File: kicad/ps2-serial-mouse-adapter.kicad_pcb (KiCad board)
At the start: 2 copper layers, 60.5 x 31.5 mm, 13 parts, among them U1 Arduino_Mini, U2 MAX232

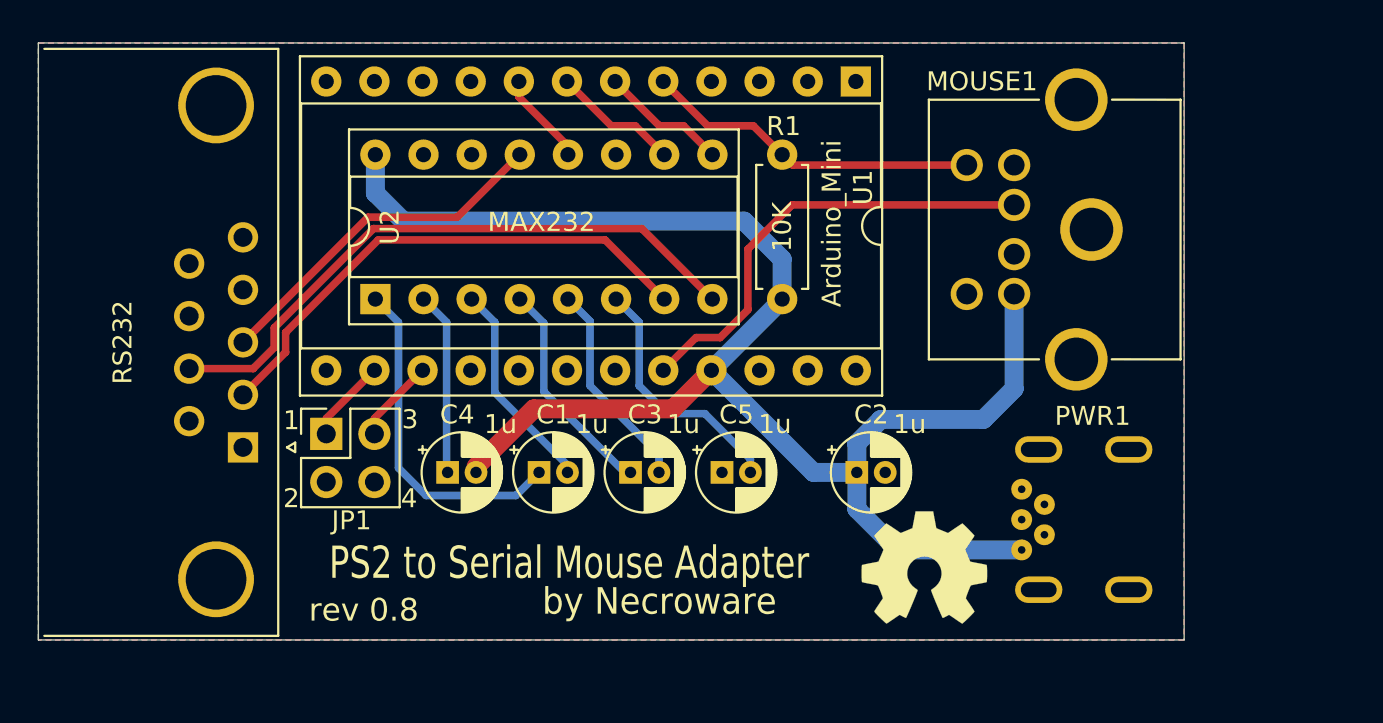
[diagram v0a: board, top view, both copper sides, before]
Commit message: Add footprints for Arduino Nano socket and MAX3232 HW-027 module
- Created a new footprint for the Arduino Nano socket with 2x15 pin configuration, including through-hole pads and silk screen details.
- Added a footprint for the MAX3232 HW-027 module featuring castellated pads, through-hole and SMD pads, along with necessary fabrication outlines.
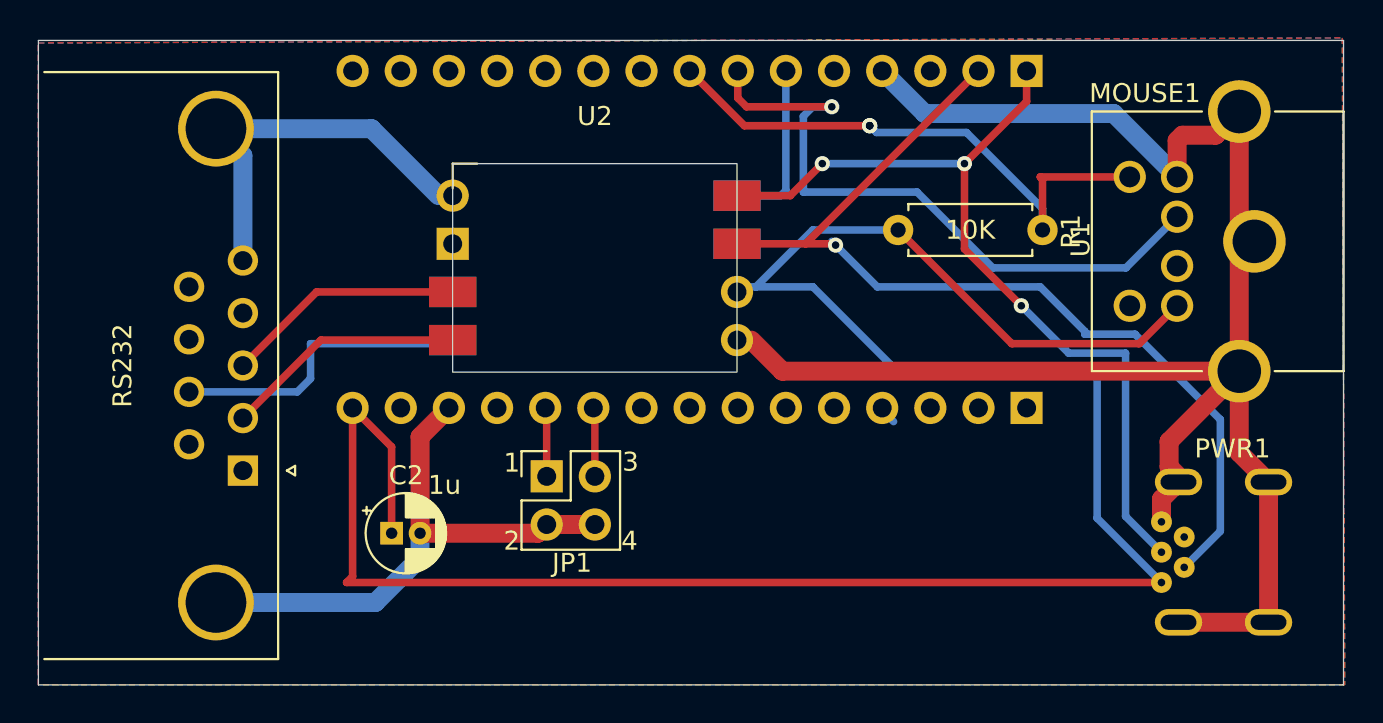
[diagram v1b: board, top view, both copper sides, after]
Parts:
- removed C1, C3, C4, C5: 1u, Capacitor_THT:CP_Radial_D4.0mm_P1.50mm
- removed REF**: OSHW-Symbol_6.7x6mm_SilkScreen, Symbol:OSHW-Symbol_6.7x6mm_SilkScreen
- U1: value Arduino_Mini -> Arduino_Nano; footprint Package_DIP:DIP-24_W15.24mm_Socket -> ps2-serial-mouse-adapter:Arduino_Nano_Socket
- U2: value MAX232 -> MAX3232_HW027; footprint Package_DIP:DIP-16_W7.62mm_Socket -> ps2-serial-mouse-adapter:MAX3232_HW027
- moved C2 24.8 mm to (99.9, 80.7)
- moved U1 12.1 mm to (115.6, 65.2)
- moved JP1 11.8 mm to (108.1, 77.7)
- moved U2 11.7 mm to (110.6, 66.7), turned to 0 degrees
- moved MOUSE1 8.62 mm to (138.9, 68.7)
- moved PWR1 7.57 mm to (140.5, 81.7)
- moved R1 7.12 mm to (126.6, 64.7), turned to 0 degrees
- moved RS232 1.23 mm to (92.1, 77.4)
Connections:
- C2 pad 1: Net-(PWR1-VBUS) -> unconnected-(C2-Pad1)
- JP1 pad 1: Net-(JP1-Pin_1) -> unconnected-(C2-Pad1)
- JP1 pad 3: Net-(JP1-Pin_3) -> unconnected-(C2-Pad1)
- MOUSE1 pad 4: Net-(PWR1-VBUS) -> unconnected-(C2-Pad1)
- PWR1 pad 1: Net-(PWR1-VBUS) -> unconnected-(C2-Pad1)
- PWR1 pad 2: unconnected-(PWR1-D--Pad2) -> RX
- PWR1 pad 3: unconnected-(PWR1-D+-Pad3) -> TX
- R1 pad 1: Net-(PWR1-VBUS) -> unconnected-(C2-Pad1)
- RS232 pad 2: Net-(U2-T2OUT) -> Net-(U2-RS232_TXD1)
- RS232 pad 3: Net-(U2-R1IN) -> Net-(U2-RS232_RXD1)
- RS232 pad 7: Net-(U2-R2IN) -> Net-(U2-RS232_RXD2)
- U1 pad 1: unconnected-(U1-TX/D0-Pad1) -> TX
- U1 pad 14: Net-(JP1-Pin_1) -> unconnected-(U1-D11-Pad14)
- U1 pad 15: Net-(JP1-Pin_3) -> unconnected-(U1-D12-Pad15)
- U1 pad 16: unconnected-(U1-D13-Pad16) -> unconnected-(C2-Pad1)
- U1 pad 17: unconnected-(U1-A0-Pad17) -> unconnected-(C2-Pad1)
- U1 pad 18: unconnected-(U1-A1-Pad18) -> unconnected-(C2-Pad1)
- U1 pad 19: unconnected-(U1-A2-Pad19) -> unconnected-(C2-Pad1)
- U1 pad 2: unconnected-(U1-RX/D1-Pad2) -> RX
- U1 pad 20: DATA -> unconnected-(C2-Pad1)
- U1 pad 21: Net-(PWR1-VBUS) -> unconnected-(C2-Pad1)
- U1 pad 22: unconnected-(U1-RST-Pad22) -> unconnected-(C2-Pad1)
- U1 pad 23: GND -> unconnected-(C2-Pad1)
- U1 pad 24: unconnected-(U1-VIN-Pad24) -> unconnected-(C2-Pad1)
- U1 pad 5: CLK -> unconnected-(U1-D2-Pad5)
- U1 pad 7: TX -> DATA
- U1 pad 8: RX -> CLK
- U2 pad 1: Net-(U2-C1+) -> unconnected-(C2-Pad1)
- U2 pad 10: TX -> RX
- U2 pad 12: RX -> RTS
- U2 pad 2: Net-(U2-VS+) -> GND
- U2 pad 3: Net-(U2-C1-) -> unconnected-(C2-Pad1)
- U2 pad 4: Net-(U2-C2+) -> GND
- U2 pad 5: Net-(U2-C2-) -> Net-(U2-RS232_RXD1)
- U2 pad 6: Net-(U2-VS-) -> Net-(U2-RS232_TXD1)
- U2 pad 7: Net-(U2-T2OUT) -> Net-(U2-RS232_RXD2)
- U2 pad 8: Net-(U2-R2IN) -> unconnected-(U2-RS232_TXD2-Pad8)
- U2 pad 9: RTS -> TX
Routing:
- net GND: track 0.00 -> 143.5 mm
- net unconnected-(C2-Pad1): track 0.00 -> 129.0 mm
- net Net-(PWR1-VBUS): track 84.3 -> 0.00 mm
- net RX: track 4.93 -> 50.7 mm, vias 0 -> 1
- net TX: track 6.73 -> 45.1 mm, vias 0 -> 3
- net Net-(U2-R2IN): track 32.8 -> 0.00 mm
- net Net-(U2-T2OUT): track 27.5 -> 0.00 mm
- net Net-(U2-R1IN): track 18.7 -> 0.00 mm
- net Net-(U2-C1+): track 17.9 -> 0.00 mm
- net Net-(U2-RS232_RXD2): track 0.00 -> 15.8 mm
- net Net-(U2-VS-): track 13.2 -> 0.00 mm
- net Net-(U2-RS232_TXD1): track 0.00 -> 12.6 mm
- net CLK: track 17.8 -> 30.3 mm, vias 0 -> 2
- net Net-(U2-RS232_RXD1): track 0.00 -> 12.2 mm
- net Net-(U2-C2+): track 11.7 -> 0.00 mm
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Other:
- board size 60.5 x 31.5 mm -> 68.9 x 34 mm
- board text removed: "PS2 to Serial Mouse Adapter"
- board text removed: "by Necroware"
- board text removed: "rev 0.8"

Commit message: Update Arduino Nano Socket footprint and adjust active layer in project file
- Changed the active layer in the project file from 2 to 0 for better visibility.
- Updated the Arduino Nano Socket footprint to a new version with enhanced properties and formatting.
- Added detailed properties for reference, value, datasheet, and description with UUIDs.
- Expanded pad definitions to include all 30 pins with consistent attributes and UUIDs.
- Improved the footprint's rectangle yard dimensions and ensured proper layer assignments.
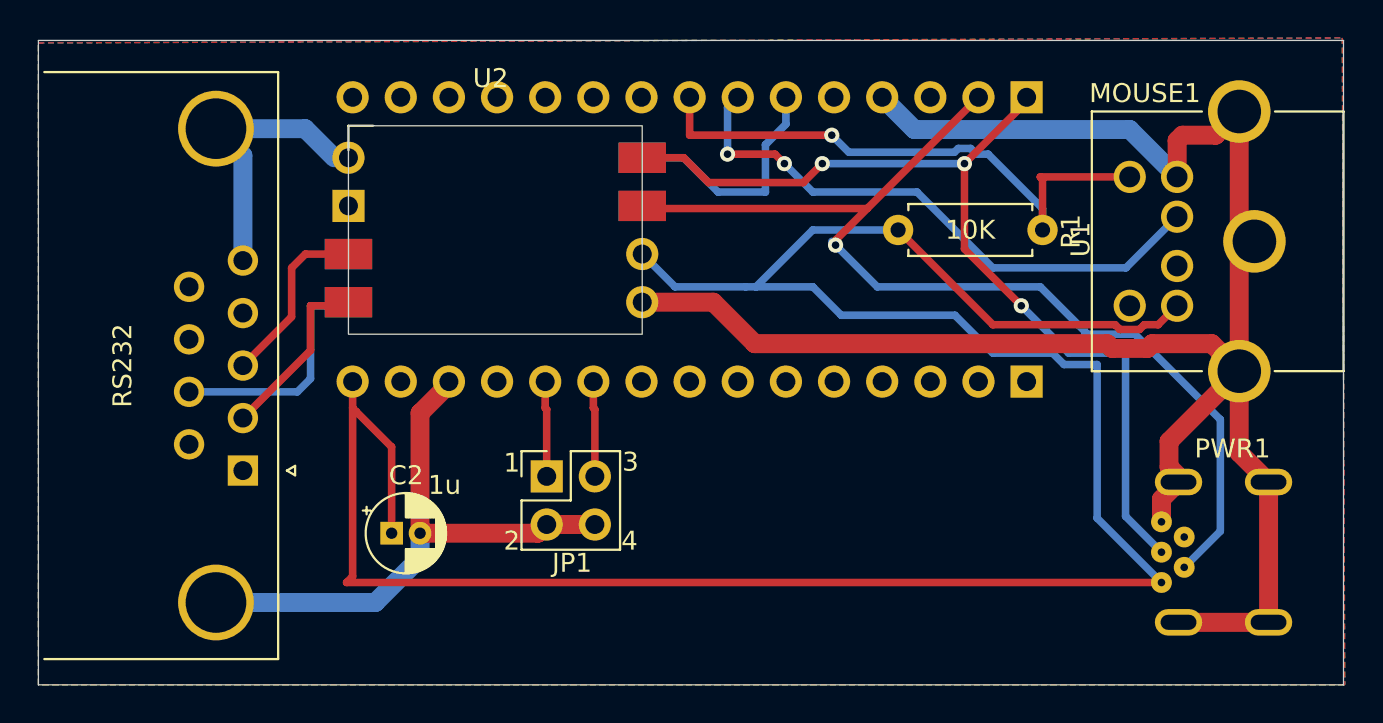
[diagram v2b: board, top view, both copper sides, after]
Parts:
- moved U2 5.85 mm to (105.1, 64.7)
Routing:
- net unconnected-(C2-Pad1): track 129.0 -> 137.2 mm
- net RX: track 50.7 -> 55.6 mm
- net RTS: track 8.55 -> 12.2 mm
- net TX: track 45.1 -> 48.7 mm
- net DATA: track 34.8 -> 31.2 mm, vias 1 -> 2
- net Net-(U2-RS232_RXD2): track 15.8 -> 12.3 mm
- net Net-(U2-RS232_TXD1): track 12.6 -> 9.39 mm
- net Net-(U2-RS232_RXD1): track 12.2 -> 9.49 mm
- net GND: track 143.5 -> 145.8 mm
- net CLK: track 30.3 -> 31.1 mm, vias 2 -> 1
